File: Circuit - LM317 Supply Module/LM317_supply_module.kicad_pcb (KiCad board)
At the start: 2 copper layers, 47.7 x 37.7 mm, 30 parts, among them J1 Conn_01x02, J2 Conn_01x02, J3 Conn_01x02, Q1 DMP4011SPSQ, Q2 2N7002, SW1 SW_SPDT, U1 LM317_SOT-223

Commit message: PCB Layout Done, DRC OK
update PCB layout, <NEED> Review Gerber file
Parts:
- added REF**: MountingHole_3.2mm_M3_ISO7380, MountingHole:MountingHole_3.2mm_M3_ISO7380, F.Cu at (181.2, 154.2)
- added REF**: MountingHole_3.2mm_M3_ISO7380, MountingHole:MountingHole_3.2mm_M3_ISO7380, F.Cu at (181.2, 123.2)
- added REF**: MountingHole_3.2mm_M3_ISO7380, MountingHole:MountingHole_3.2mm_M3_ISO7380, F.Cu at (222.2, 138.5)
- moved C4 152.0 mm to (216.1, 154.1)
- moved C2 145.6 mm to (191.3, 149.2)
- moved D5 145.6 mm to (183.5, 142.1)
- moved Q1 145.6 mm to (198.4, 137.1)
- moved Q2 145.6 mm to (208.4, 138.1)
- moved R1 145.6 mm to (202.0, 124.2)
- moved R10 145.6 mm to (186.9, 142.1)
- moved R2 145.6 mm to (204.8, 129.7)
- moved R5 145.6 mm to (207.4, 142.6)
- moved R6 145.6 mm to (203.6, 140.7)
- moved RV1 145.6 mm to (215.9, 125.9)
- moved C1 145.6 mm to (202.8, 137.9)
- moved C3 145.6 mm to (186.9, 143.9)
- moved D1 145.6 mm to (200.2, 128.2)
- moved D2 145.6 mm to (204.2, 142.8)
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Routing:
- net Net-(D2-A): track 6.76 -> 7.91 mm
- net Net-(D2-K): track 6.78 -> 7.73 mm
- net Net-(SW1-C): track 10.2 -> 9.52 mm
- net Earth: vias 0 -> 7
- added copper zone on F.Cu, net /VIN
- added copper zone on F.Cu, net /VOUT
- added copper zone on B.Cu, net Earth
- added copper zone on F.Cu, net Earth
- added copper zone on F.Cu, net Net-(D3-A)
- added copper zone on F.Cu, net Net-(D3-K)
- added copper zone on F.Cu, net Net-(U1-ADJ)
- added copper zone on F.Cu, net Net-(U1-VI)

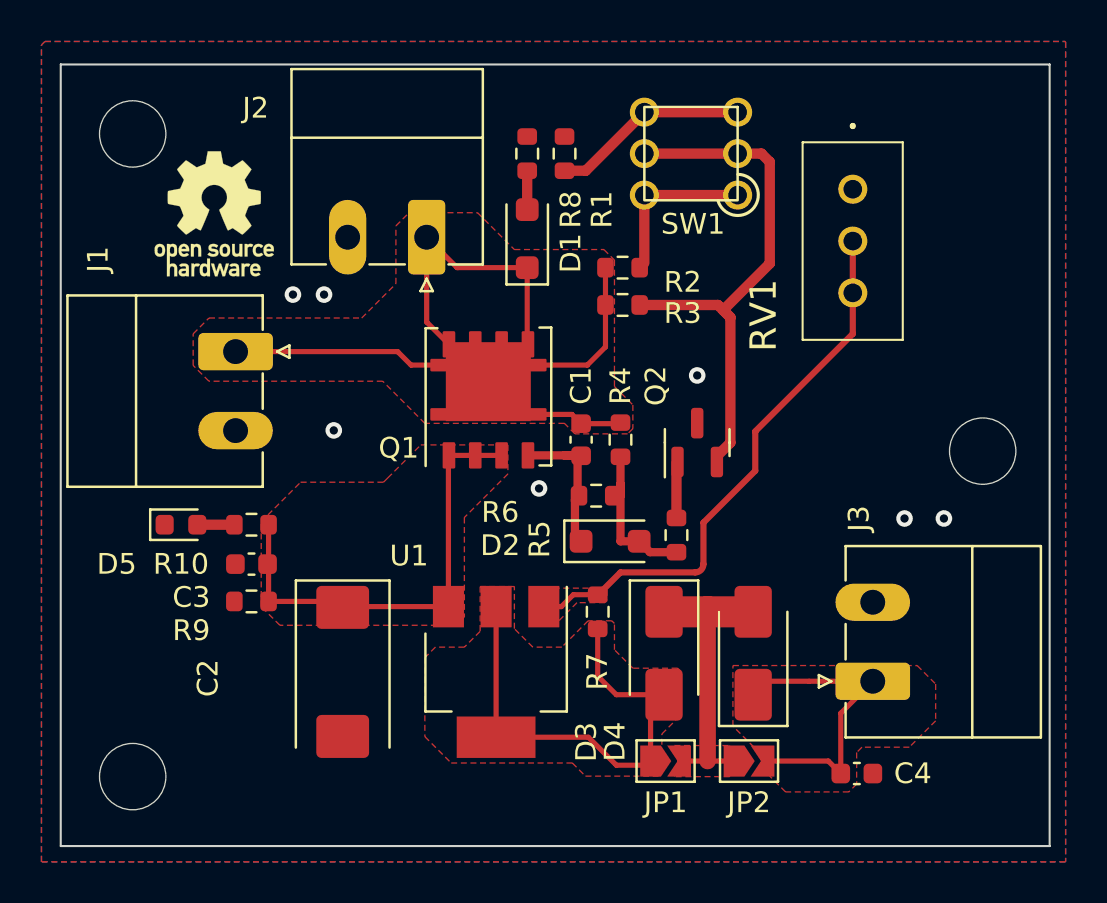
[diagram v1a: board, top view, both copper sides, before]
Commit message: Modify Single Layer PCB
modify input/output connector & LED size
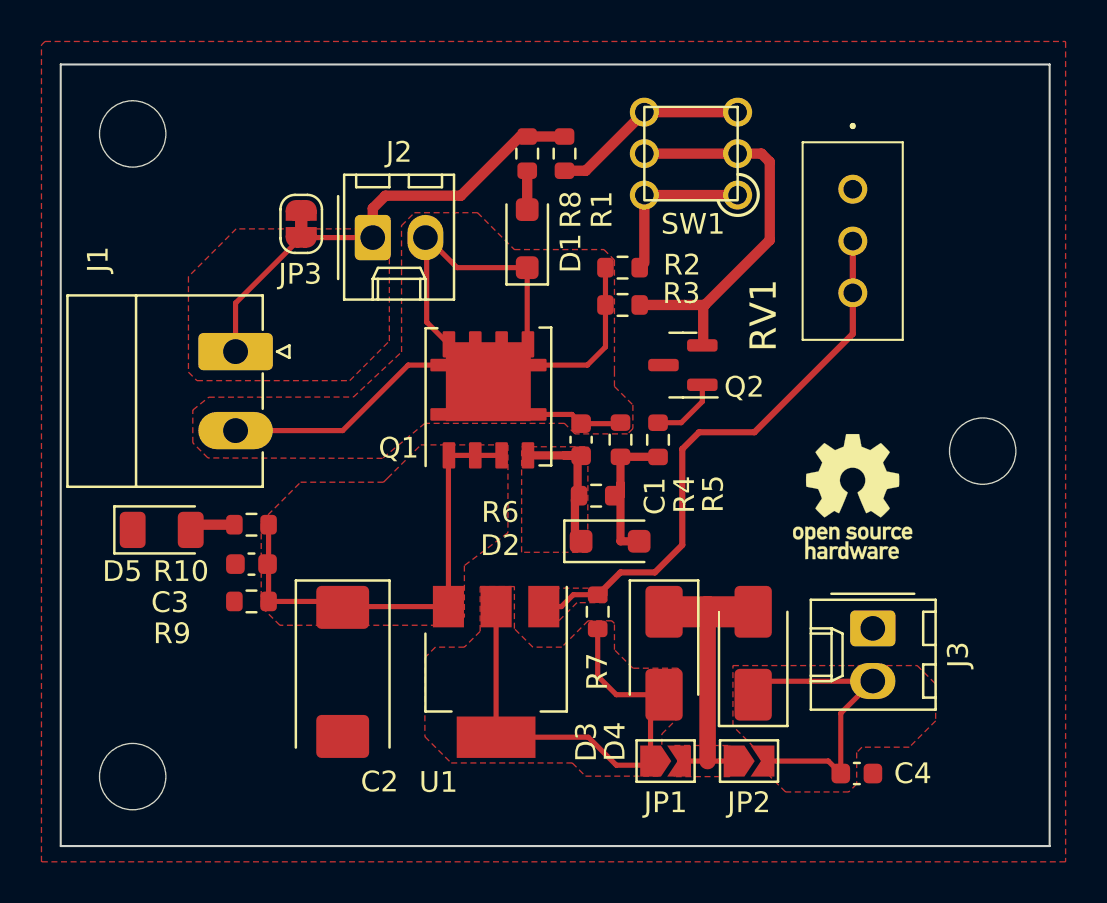
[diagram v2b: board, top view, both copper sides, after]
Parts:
- added JP3: SolderJumper_2_Bridged, Jumper:SolderJumper-2_P1.3mm_Bridged_RoundedPad1.0x1.5mm, F.Cu at (189.3, 127.5)
- D5: footprint LED_SMD:LED_0603_1608Metric -> LED_SMD:LED_1206_3216Metric
- J2, J3: footprint Connector_Phoenix_MC:PhoenixContact_MC_1,5_2-G-3.81_1x02_P3.81mm_Horizontal -> Connector_Molex:Molex_KK-254_AE-6410-02A_1x02_P2.54mm_Vertical
- moved REF** 33.7 mm to (215.9, 140.7)
- moved R5 4.68 mm to (206.5, 138.0)
- moved Q2 3.80 mm to (207.7, 134.3), turned to 180 degrees
- moved J2 2.60 mm to (192.8, 128.2), turned to 0 degrees
- moved J3 2.55 mm to (216.9, 147.1), turned to -90 degrees
- moved D5 0.96 mm to (182.6, 142.3)
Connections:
- C2 pad 2: Earth -> GNDREF
- C3 pad 2: Earth -> GNDREF
- C4 pad 2: Earth -> GNDREF
- D5 pad 1: Earth -> GNDREF
- J1 pad 1: /VIN -> Earth
- J1 pad 2: Earth -> /VIN
- J2 pad 1: /VIN -> Earth
- J2 pad 2: Earth -> /VIN
- J3 pad 1: /VOUT -> GNDREF
- J3 pad 2: Earth -> /VOUT
- Q2 pad 3: Earth -> GNDREF
- R9 pad 2: Earth -> GNDREF
- RV1 pad 1: Earth -> GNDREF
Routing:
- net Earth: track 0.00 -> 22.4 mm, vias 7 -> 0
- net Net-(Q2-G): track 26.7 -> 19.5 mm
- net /VIN: track 37.1 -> 38.2 mm
- net Net-(Q2-D): track 2.72 -> 3.37 mm
- added copper zone on F.Cu, net GNDREF
- added copper zone on F.Cu, net Net-(D2-K)
- removed copper zone on B.Cu, net Earth
